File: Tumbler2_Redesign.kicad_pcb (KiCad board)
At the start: 2 copper layers, 77 x 84 mm, 4 parts

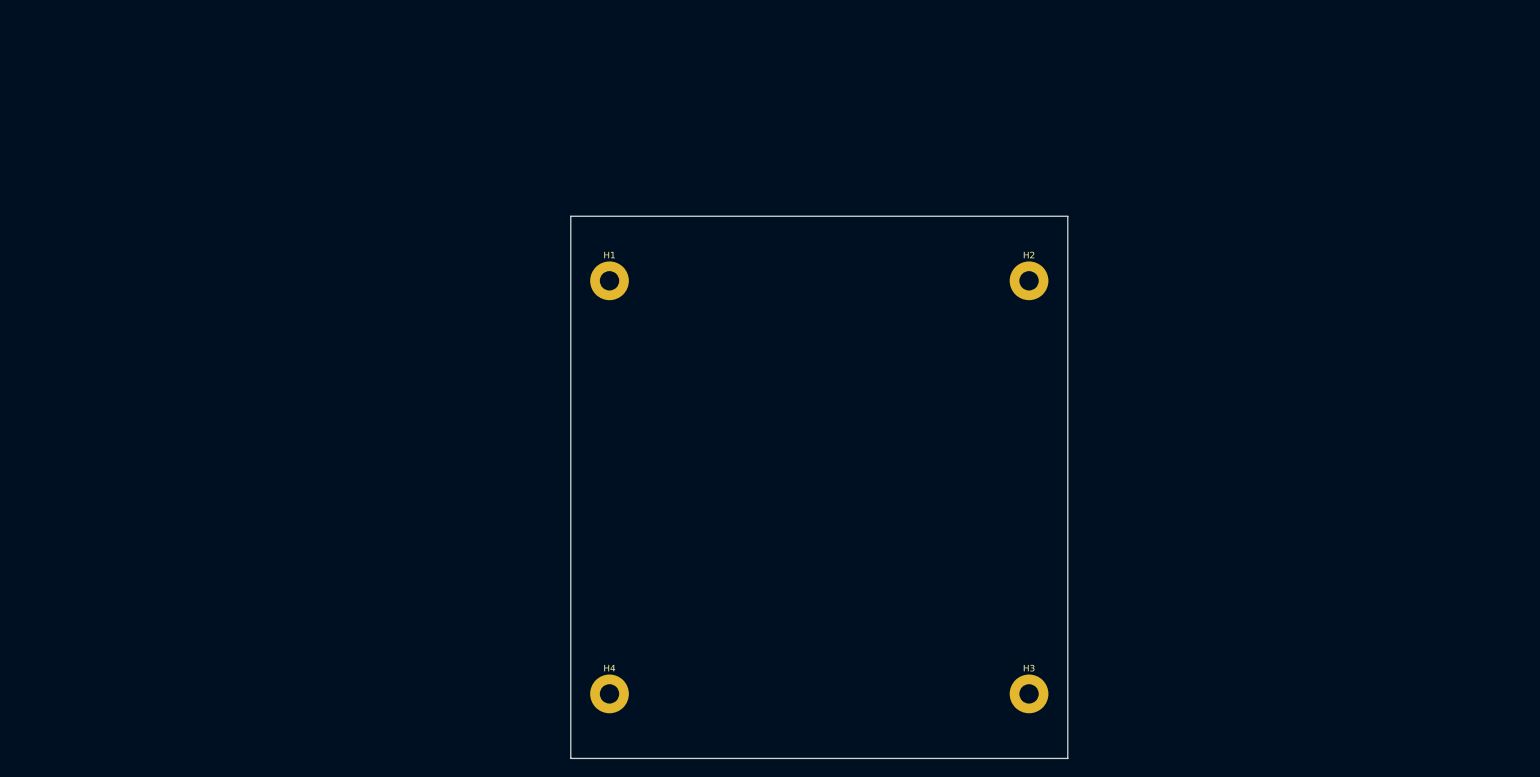
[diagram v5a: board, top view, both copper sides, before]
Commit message: Add components to layout
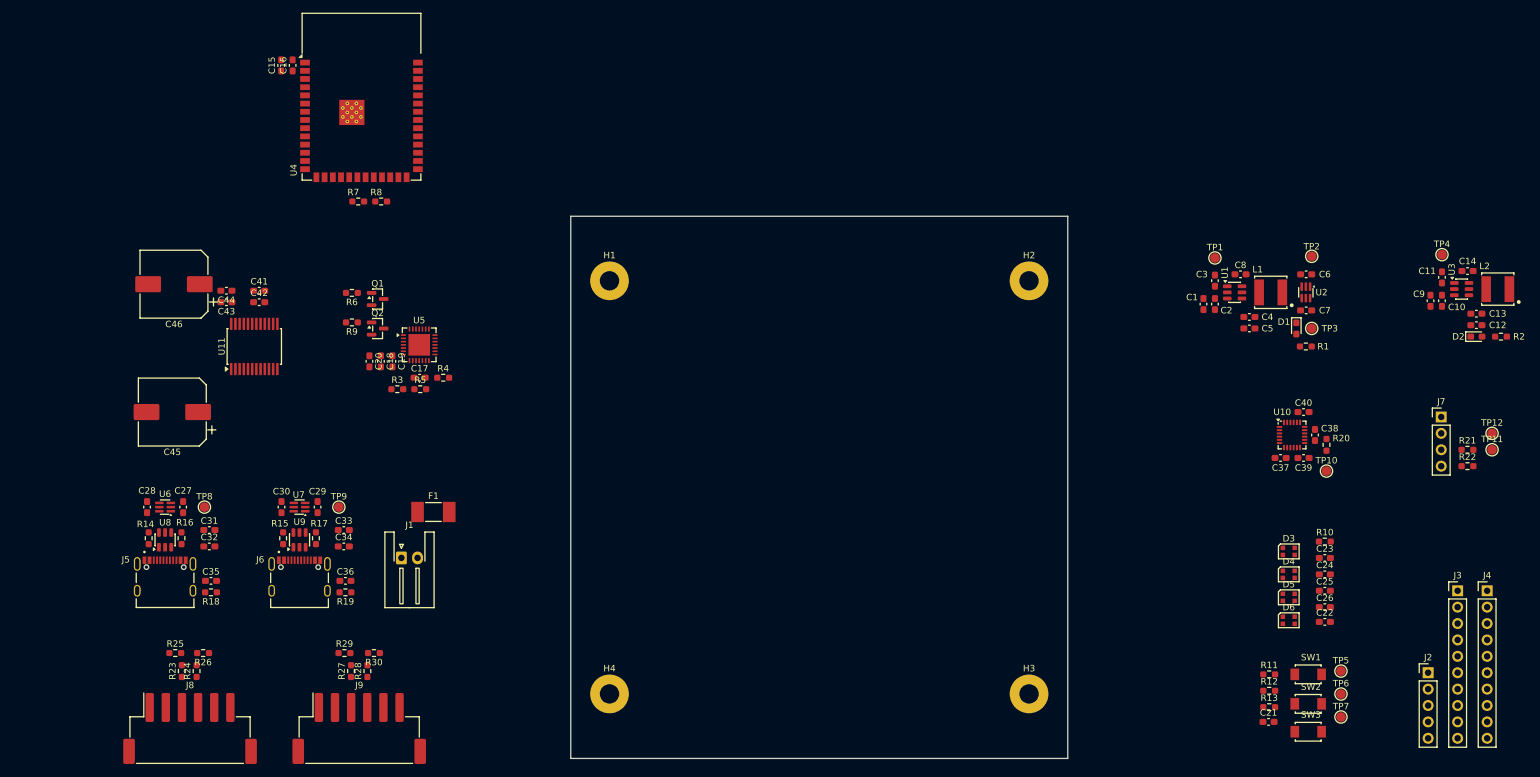
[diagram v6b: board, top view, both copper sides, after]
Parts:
- added C1: 10uF, Capacitor_SMD:C_0603_1608Metric_Pad1.08x0.95mm_HandSolder, F.Cu at (211.8, 75.0)
- added C10: 100nF, Capacitor_SMD:C_0603_1608Metric_Pad1.08x0.95mm_HandSolder, F.Cu at (248.8, 74.5)
- added C11: 100nF, Capacitor_SMD:C_0603_1608Metric_Pad1.08x0.95mm_HandSolder, F.Cu at (248.8, 70.8)
- added C12: 22uF, Capacitor_SMD:C_0603_1608Metric_Pad1.08x0.95mm_HandSolder, F.Cu at (254.1, 78.2)
- added C13: 22uF, Capacitor_SMD:C_0603_1608Metric_Pad1.08x0.95mm_HandSolder, F.Cu at (254.1, 76.5)
- added C14: 100nF, Capacitor_SMD:C_0603_1608Metric_Pad1.08x0.95mm_HandSolder, F.Cu at (252.7, 69.8)
- added C15: 10uF, Capacitor_SMD:C_0603_1608Metric_Pad1.08x0.95mm_HandSolder, F.Cu at (68.9, 38.0)
- added C16: 100nF, Capacitor_SMD:C_0603_1608Metric_Pad1.08x0.95mm_HandSolder, F.Cu at (70.7, 38.0)
- added C17: 1uF, Capacitor_SMD:C_0603_1608Metric_Pad1.08x0.95mm_HandSolder, F.Cu at (90.4, 86.4)
- added C18: 100nF, Capacitor_SMD:C_0603_1608Metric_Pad1.08x0.95mm_HandSolder, F.Cu at (84.4, 83.8)
- added C19: 100nF, Capacitor_SMD:C_0603_1608Metric_Pad1.08x0.95mm_HandSolder, F.Cu at (86.2, 83.8)
- added C2: 100nF, Capacitor_SMD:C_0603_1608Metric_Pad1.08x0.95mm_HandSolder, F.Cu at (213.6, 75.0)
- added C20: 10uF, Capacitor_SMD:C_0603_1608Metric_Pad1.08x0.95mm_HandSolder, F.Cu at (82.6, 83.8)
- added C21: 1uF, Capacitor_SMD:C_0603_1608Metric_Pad1.08x0.95mm_HandSolder, F.Cu at (221.9, 139.7)
- added C22: 100nF, Capacitor_SMD:C_0603_1608Metric_Pad1.08x0.95mm_HandSolder, F.Cu at (230.6, 124.2)
- added C23: 100nF, Capacitor_SMD:C_0603_1608Metric_Pad1.08x0.95mm_HandSolder, F.Cu at (230.6, 114.3)
- added C24: 100nF, Capacitor_SMD:C_0603_1608Metric_Pad1.08x0.95mm_HandSolder, F.Cu at (230.6, 116.8)
- added C25: 100nF, Capacitor_SMD:C_0603_1608Metric_Pad1.08x0.95mm_HandSolder, F.Cu at (230.6, 119.4)
- added C26: 10uF, Capacitor_SMD:C_0603_1608Metric_Pad1.08x0.95mm_HandSolder, F.Cu at (230.6, 121.9)
- added C27: 100nF, Capacitor_SMD:C_0603_1608Metric_Pad1.08x0.95mm_HandSolder, F.Cu at (53.7, 106.4)
- added C28: 100nF, Capacitor_SMD:C_0603_1608Metric_Pad1.08x0.95mm_HandSolder, F.Cu at (48.2, 106.4)
- added C29: 100nF, Capacitor_SMD:C_0603_1608Metric_Pad1.08x0.95mm_HandSolder, F.Cu at (74.6, 106.4)
- added C3: 100nF, Capacitor_SMD:C_0603_1608Metric_Pad1.08x0.95mm_HandSolder, F.Cu at (213.6, 71.3)
- added C30: 100nF, Capacitor_SMD:C_0603_1608Metric_Pad1.08x0.95mm_HandSolder, F.Cu at (69.0, 106.4)
- added C31: 100nF, Capacitor_SMD:C_0603_1608Metric_Pad1.08x0.95mm_HandSolder, F.Cu at (57.8, 110.0)
- added C32: 10uF, Capacitor_SMD:C_0603_1608Metric_Pad1.08x0.95mm_HandSolder, F.Cu at (57.8, 112.5)
- added C33: 100nF, Capacitor_SMD:C_0603_1608Metric_Pad1.08x0.95mm_HandSolder, F.Cu at (78.6, 110.0)
- added C34: 10uF, Capacitor_SMD:C_0603_1608Metric_Pad1.08x0.95mm_HandSolder, F.Cu at (78.6, 112.5)
- added C35: 100nF, Capacitor_SMD:C_0603_1608Metric_Pad1.08x0.95mm_HandSolder, F.Cu at (58.1, 117.8)
- added C36: 100nF, Capacitor_SMD:C_0603_1608Metric_Pad1.08x0.95mm_HandSolder, F.Cu at (78.9, 117.8)
- added C37: 100nF, Capacitor_SMD:C_0603_1608Metric_Pad1.08x0.95mm_HandSolder, F.Cu at (223.8, 98.8)
- added C38: 10nF, Capacitor_SMD:C_0603_1608Metric_Pad1.08x0.95mm_HandSolder, F.Cu at (229.1, 95.2)
- added C39: 100nF, Capacitor_SMD:C_0603_1608Metric_Pad1.08x0.95mm_HandSolder, F.Cu at (227.3, 98.8)
- added C4: 22uF, Capacitor_SMD:C_0603_1608Metric_Pad1.08x0.95mm_HandSolder, F.Cu at (218.9, 77.0)
- added C40: 2.2nF, Capacitor_SMD:C_0603_1608Metric_Pad1.08x0.95mm_HandSolder, F.Cu at (227.3, 91.7)
- added C41: 10uF, Capacitor_SMD:C_0603_1608Metric_Pad1.08x0.95mm_HandSolder, F.Cu at (65.5, 72.9)
- added C42: 100nF, Capacitor_SMD:C_0603_1608Metric_Pad1.08x0.95mm_HandSolder, F.Cu at (65.5, 74.7)
- added C43: 100nF, Capacitor_SMD:C_0603_1608Metric_Pad1.08x0.95mm_HandSolder, F.Cu at (60.5, 74.7)
- added C44: 10uF, Capacitor_SMD:C_0603_1608Metric_Pad1.08x0.95mm_HandSolder, F.Cu at (60.5, 72.9)
- added C45: 220uF, Capacitor_SMD:CP_Elec_10x10, F.Cu at (52.1, 91.7)
- added C46: 220uF, Capacitor_SMD:CP_Elec_10x10, F.Cu at (52.3, 71.9)
- added C5: 22uF, Capacitor_SMD:C_0603_1608Metric_Pad1.08x0.95mm_HandSolder, F.Cu at (218.9, 78.7)
- added C6: 100nF, Capacitor_SMD:C_0603_1608Metric_Pad1.08x0.95mm_HandSolder, F.Cu at (227.7, 70.4)
- added C7: 100nF, Capacitor_SMD:C_0603_1608Metric_Pad1.08x0.95mm_HandSolder, F.Cu at (227.7, 75.9)
- added C8: 100nF, Capacitor_SMD:C_0603_1608Metric_Pad1.08x0.95mm_HandSolder, F.Cu at (217.6, 70.4)
- added C9: 10uF, Capacitor_SMD:C_0603_1608Metric_Pad1.08x0.95mm_HandSolder, F.Cu at (247.0, 74.5)
- added D1: LED, LED_SMD:LED_0603_1608Metric_Pad1.05x0.95mm_HandSolder, F.Cu at (226.2, 78.7)
- added D2: LED, LED_SMD:LED_0603_1608Metric_Pad1.05x0.95mm_HandSolder, F.Cu at (254.1, 80.0)
- added D3: WS2812B, LED_SMD:LED_WS2812B-2020_PLCC4_2.0x2.0mm, F.Cu at (225.0, 113.3)
- added D4: WS2812B, LED_SMD:LED_WS2812B-2020_PLCC4_2.0x2.0mm, F.Cu at (225.0, 116.8)
- added D5: WS2812B, LED_SMD:LED_WS2812B-2020_PLCC4_2.0x2.0mm, F.Cu at (225.0, 120.4)
- added D6: WS2812B, LED_SMD:LED_WS2812B-2020_PLCC4_2.0x2.0mm, F.Cu at (225.0, 124.0)
- added F1: 5A, Fuse:Fuse_Littelfuse-NANO2-451_453, F.Cu at (92.5, 107.2)
- added J1: Conn_01x02, Connector_JST:JST_XH_S2B-XH-A-1_1x02_P2.50mm_Horizontal, F.Cu at (87.6, 114.3)
- added J2: Conn_01x05, Connector_PinHeader_2.54mm:PinHeader_1x05_P2.54mm_Vertical, F.Cu at (246.6, 132.1)
- added J3: Conn_01x10, Connector_PinHeader_2.54mm:PinHeader_1x10_P2.54mm_Vertical, F.Cu at (251.2, 119.4)
- added J4: Conn_01x10, Connector_PinHeader_2.54mm:PinHeader_1x10_P2.54mm_Vertical, F.Cu at (255.8, 119.4)
- added J5: USB_C_Receptacle_USB2.0_16P, Tumbler2:KINGHELM_KH-TYPE-C-16P, F.Cu at (51.0, 119.4)
- added J6: USB_C_Receptacle_USB2.0_16P, Tumbler2:KINGHELM_KH-TYPE-C-16P, F.Cu at (71.8, 119.4)
- added J7: Conn_01x04, Connector_PinHeader_2.54mm:PinHeader_1x04_P2.54mm_Vertical, F.Cu at (248.7, 92.5)
- added J8: Conn_01x06, Connector_JST:JST_XH_S6B-XH-SM4-TB_1x06-1MP_P2.50mm_Horizontal, F.Cu at (54.8, 140.7)
- added J9: Conn_01x06, Connector_JST:JST_XH_S6B-XH-SM4-TB_1x06-1MP_P2.50mm_Horizontal, F.Cu at (81.0, 140.7)
- added L1: 4.7uH, Tumbler2:VLS5045EX-4R7M, F.Cu at (222.2, 73.2)
- added L2: 4.7uH, Tumbler2:VLS5045EX-4R7M, F.Cu at (257.4, 72.6)
- added Q1: BC817, Package_TO_SOT_SMD:SOT-23, F.Cu at (83.9, 74.2)
- added Q2: BC817, Package_TO_SOT_SMD:SOT-23, F.Cu at (83.9, 78.8)
- added R1: 680, Resistor_SMD:R_0603_1608Metric_Pad0.98x0.95mm_HandSolder, F.Cu at (227.7, 81.5)
- added R10: 10k, Resistor_SMD:R_0603_1608Metric_Pad0.98x0.95mm_HandSolder, F.Cu at (230.6, 111.8)
- added R11: 10k, Resistor_SMD:R_0603_1608Metric_Pad0.98x0.95mm_HandSolder, F.Cu at (222.0, 132.3)
- added R12: 10k, Resistor_SMD:R_0603_1608Metric_Pad0.98x0.95mm_HandSolder, F.Cu at (222.0, 134.9)
- added R13: 10k, Resistor_SMD:R_0603_1608Metric_Pad0.98x0.95mm_HandSolder, F.Cu at (222.0, 137.4)
- added R14: 5k1, Resistor_SMD:R_0603_1608Metric_Pad0.98x0.95mm_HandSolder, F.Cu at (48.4, 111.2)
- added R15: 5k1, Resistor_SMD:R_0603_1608Metric_Pad0.98x0.95mm_HandSolder, F.Cu at (69.2, 111.2)
- added R16: 5k1, Resistor_SMD:R_0603_1608Metric_Pad0.98x0.95mm_HandSolder, F.Cu at (53.5, 111.2)
- added R17: 5k1, Resistor_SMD:R_0603_1608Metric_Pad0.98x0.95mm_HandSolder, F.Cu at (74.3, 111.2)
- added R18: 1M, Resistor_SMD:R_0603_1608Metric_Pad0.98x0.95mm_HandSolder, F.Cu at (58.1, 119.6)
- added R19: 1M, Resistor_SMD:R_0603_1608Metric_Pad0.98x0.95mm_HandSolder, F.Cu at (78.9, 119.6)
- added R2: 470, Resistor_SMD:R_0603_1608Metric_Pad0.98x0.95mm_HandSolder, F.Cu at (257.9, 80.0)
- added R20: 10k, Resistor_SMD:R_0603_1608Metric_Pad0.98x0.95mm_HandSolder, F.Cu at (230.9, 96.8)
- added R21: 1k8, Resistor_SMD:R_0603_1608Metric_Pad0.98x0.95mm_HandSolder, F.Cu at (252.7, 97.5)
- added R22: 3k3, Resistor_SMD:R_0603_1608Metric_Pad0.98x0.95mm_HandSolder, F.Cu at (252.7, 100.1)
- added R23: 1k8, Resistor_SMD:R_0603_1608Metric_Pad0.98x0.95mm_HandSolder, F.Cu at (53.5, 131.8)
- added R24: 1k8, Resistor_SMD:R_0603_1608Metric_Pad0.98x0.95mm_HandSolder, F.Cu at (55.8, 131.8)
- added R25: 3k3, Resistor_SMD:R_0603_1608Metric_Pad0.98x0.95mm_HandSolder, F.Cu at (52.5, 129.0)
- added R26: 3k3, Resistor_SMD:R_0603_1608Metric_Pad0.98x0.95mm_HandSolder, F.Cu at (56.8, 129.0)
- added R27: 1k8, Resistor_SMD:R_0603_1608Metric_Pad0.98x0.95mm_HandSolder, F.Cu at (79.8, 131.8)
- added R28: 1k8, Resistor_SMD:R_0603_1608Metric_Pad0.98x0.95mm_HandSolder, F.Cu at (82.3, 131.8)
- added R29: 3k3, Resistor_SMD:R_0603_1608Metric_Pad0.98x0.95mm_HandSolder, F.Cu at (78.7, 129.0)
- added R3: 22k1, Resistor_SMD:R_0603_1608Metric_Pad0.98x0.95mm_HandSolder, F.Cu at (86.9, 88.2)
- added R30: 3k3, Resistor_SMD:R_0603_1608Metric_Pad0.98x0.95mm_HandSolder, F.Cu at (83.3, 129.0)
- added R4: 1k, Resistor_SMD:R_0603_1608Metric_Pad0.98x0.95mm_HandSolder, F.Cu at (94.0, 86.4)
- added R5: 47k5, Resistor_SMD:R_0603_1608Metric_Pad0.98x0.95mm_HandSolder, F.Cu at (90.5, 88.2)
- added R6: 10k, Resistor_SMD:R_0603_1608Metric_Pad0.98x0.95mm_HandSolder, F.Cu at (79.9, 73.2)
- added R7: 4k7, Resistor_SMD:R_0603_1608Metric_Pad0.98x0.95mm_HandSolder, F.Cu at (80.9, 59.1)
- added R8: 4k7, Resistor_SMD:R_0603_1608Metric_Pad0.98x0.95mm_HandSolder, F.Cu at (84.4, 59.1)
- added R9: 10k, Resistor_SMD:R_0603_1608Metric_Pad0.98x0.95mm_HandSolder, F.Cu at (79.9, 77.8)
- added SW1: SW_Push, Tumbler2:SW_TS-1088-AR02016, F.Cu at (228.0, 132.3)
- added SW2: SW_Push, Tumbler2:SW_TS-1088-AR02016, F.Cu at (228.0, 136.9)
- added SW3: SW_Push, Tumbler2:SW_TS-1088-AR02016, F.Cu at (228.0, 141.2)
- added TP1: TestPoint, TestPoint:TestPoint_Pad_D1.5mm, F.Cu at (213.6, 67.8)
- added TP10: TestPoint, TestPoint:TestPoint_Pad_D1.5mm, F.Cu at (230.9, 100.8)
- added TP11: TestPoint, TestPoint:TestPoint_Pad_D1.5mm, F.Cu at (256.5, 97.5)
- added TP12: TestPoint, TestPoint:TestPoint_Pad_D1.5mm, F.Cu at (256.5, 95.0)
- added TP2: TestPoint, TestPoint:TestPoint_Pad_D1.5mm, F.Cu at (228.6, 67.6)
- added TP3: TestPoint, TestPoint:TestPoint_Pad_D1.5mm, F.Cu at (228.6, 78.7)
- added TP4: TestPoint, TestPoint:TestPoint_Pad_D1.5mm, F.Cu at (248.8, 67.3)
- added TP5: TestPoint, TestPoint:TestPoint_Pad_D1.5mm, F.Cu at (233.1, 131.8)
- added TP6: TestPoint, TestPoint:TestPoint_Pad_D1.5mm, F.Cu at (233.1, 135.4)
- added TP7: TestPoint, TestPoint:TestPoint_Pad_D1.5mm, F.Cu at (233.1, 138.9)
- added TP8: TestPoint, TestPoint:TestPoint_Pad_D1.5mm, F.Cu at (57.0, 106.4)
- added TP9: TestPoint, TestPoint:TestPoint_Pad_D1.5mm, F.Cu at (77.9, 106.4)
- added U1: AP63205WU, Package_TO_SOT_SMD:TSOT-23-6, F.Cu at (216.7, 73.2)
- added U10: MPU-6050, Sensor_Motion:InvenSense_QFN-24_4x4mm_P0.5mm, F.Cu at (225.6, 95.2)
- added U11: TB6612FNG, Package_SO:SSOP-24_5.3x8.2mm_P0.65mm, F.Cu at (64.8, 81.5)
- added U2: LM66100DCK, Package_TO_SOT_SMD:SOT-363_SC-70-6, F.Cu at (227.7, 73.2)
- added U3: AP63203WU, Package_TO_SOT_SMD:TSOT-23-6, F.Cu at (251.8, 72.6)
- added U4: ESP32-S3-WROOM-1, RF_Module:ESP32-S3-WROOM-1, F.Cu at (81.4, 42.8)
- added U5: CP2102N-A02-GQFN28R, Package_DFN_QFN:QFN-28-1EP_5x5mm_P0.5mm_EP3.35x3.35mm, F.Cu at (90.3, 81.3)
- added U6: LM66100DCK, Package_TO_SOT_SMD:SOT-363_SC-70-6, F.Cu at (51.0, 106.4)
- added U7: LM66100DCK, Package_TO_SOT_SMD:SOT-363_SC-70-6, F.Cu at (71.8, 106.4)
- added U8: USBLC6-2SC6, Package_TO_SOT_SMD:SOT-23-6, F.Cu at (51.0, 111.5)
- added U9: USBLC6-2SC6, Package_TO_SOT_SMD:SOT-23-6, F.Cu at (71.8, 111.5)

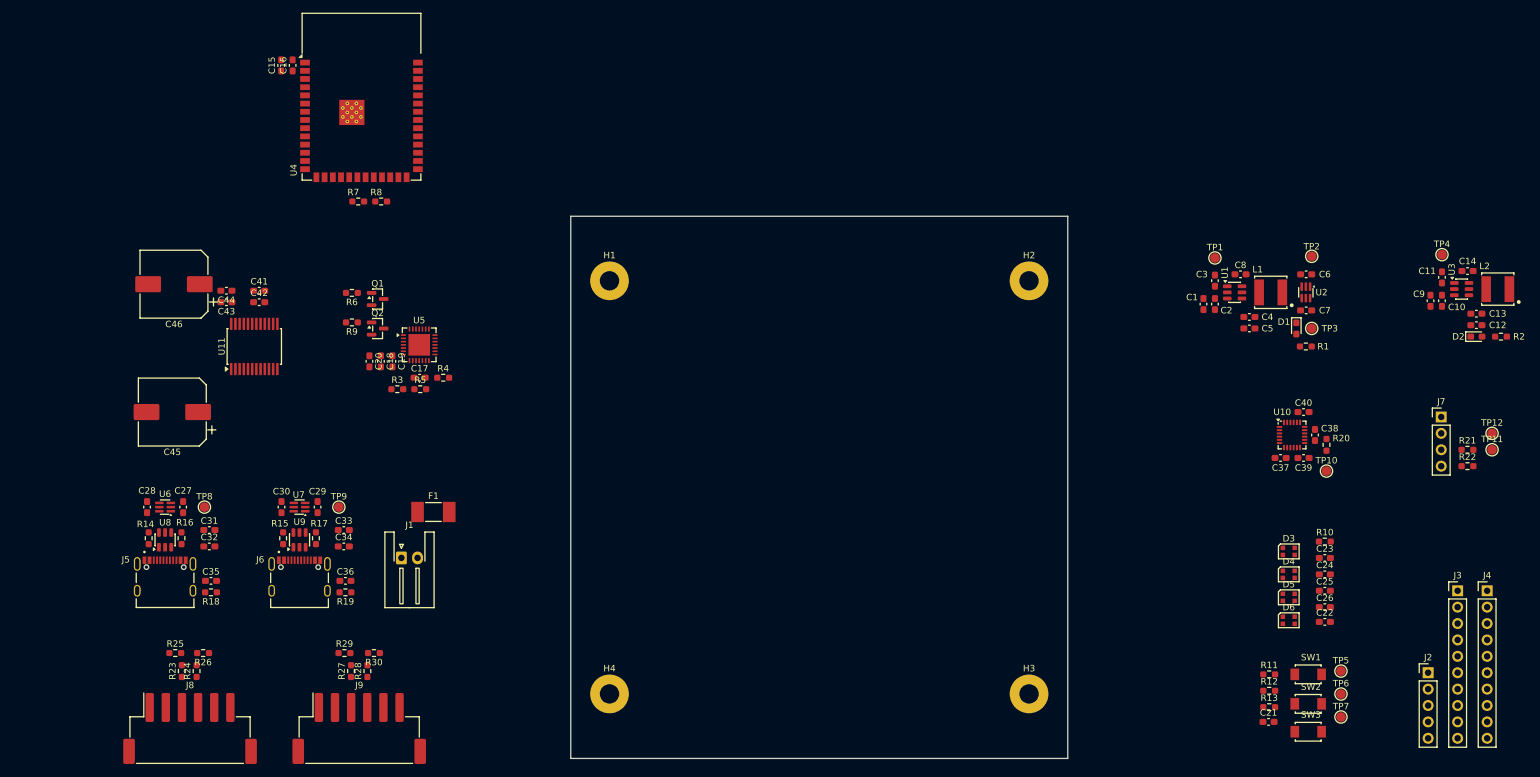
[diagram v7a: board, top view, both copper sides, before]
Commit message: Add missing rgb leds
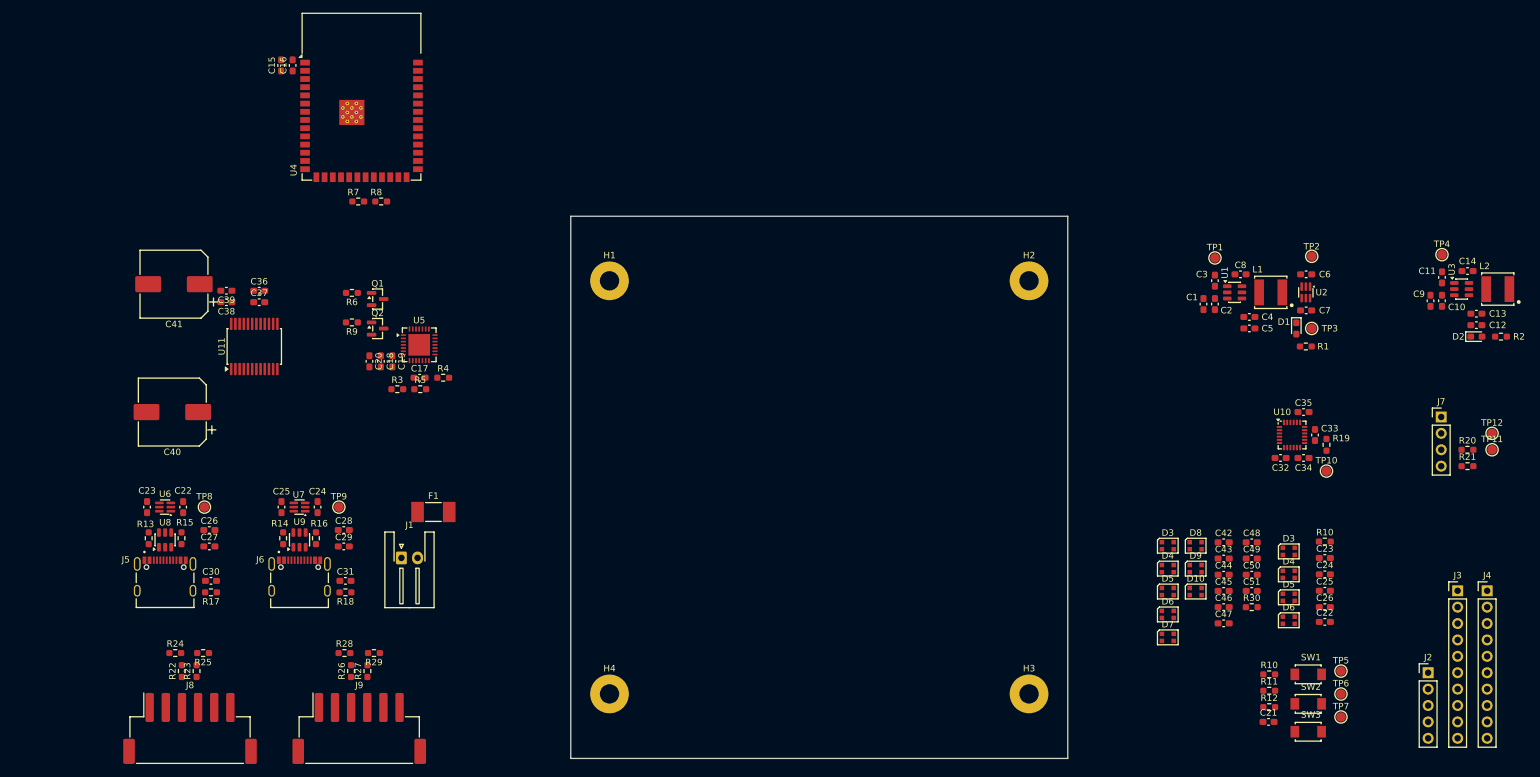
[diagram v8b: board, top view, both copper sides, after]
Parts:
- added C42: 100nF, Capacitor_SMD:C_0603_1608Metric_Pad1.08x0.95mm_HandSolder, F.Cu at (215.0, 111.9)
- added C43: 100nF, Capacitor_SMD:C_0603_1608Metric_Pad1.08x0.95mm_HandSolder, F.Cu at (215.0, 114.4)
- added C44: 100nF, Capacitor_SMD:C_0603_1608Metric_Pad1.08x0.95mm_HandSolder, F.Cu at (215.0, 116.9)
- added C45: 100nF, Capacitor_SMD:C_0603_1608Metric_Pad1.08x0.95mm_HandSolder, F.Cu at (215.0, 119.4)
- added C46: 10uF, Capacitor_SMD:C_0603_1608Metric_Pad1.08x0.95mm_HandSolder, F.Cu at (215.0, 121.9)
- added C47: 100nF, Capacitor_SMD:C_0603_1608Metric_Pad1.08x0.95mm_HandSolder, F.Cu at (215.0, 124.4)
- added C48: 100nF, Capacitor_SMD:C_0603_1608Metric_Pad1.08x0.95mm_HandSolder, F.Cu at (219.3, 111.9)
- added C49: 100nF, Capacitor_SMD:C_0603_1608Metric_Pad1.08x0.95mm_HandSolder, F.Cu at (219.3, 114.4)
- added C50: 100nF, Capacitor_SMD:C_0603_1608Metric_Pad1.08x0.95mm_HandSolder, F.Cu at (219.3, 116.9)
- added C51: 10uF, Capacitor_SMD:C_0603_1608Metric_Pad1.08x0.95mm_HandSolder, F.Cu at (219.3, 119.4)
- added D10: WS2812B, LED_SMD:LED_WS2812B-2020_PLCC4_2.0x2.0mm, F.Cu at (210.6, 119.5)
- added D3: WS2812B, LED_SMD:LED_WS2812B-2020_PLCC4_2.0x2.0mm, F.Cu at (206.3, 112.4)
- added D4: WS2812B, LED_SMD:LED_WS2812B-2020_PLCC4_2.0x2.0mm, F.Cu at (206.3, 116.0)
- added D5: WS2812B, LED_SMD:LED_WS2812B-2020_PLCC4_2.0x2.0mm, F.Cu at (206.3, 119.5)
- added D6: WS2812B, LED_SMD:LED_WS2812B-2020_PLCC4_2.0x2.0mm, F.Cu at (206.3, 123.0)
- added D7: WS2812B, LED_SMD:LED_WS2812B-2020_PLCC4_2.0x2.0mm, F.Cu at (206.3, 126.6)
- added D8: WS2812B, LED_SMD:LED_WS2812B-2020_PLCC4_2.0x2.0mm, F.Cu at (210.6, 112.4)
- added D9: WS2812B, LED_SMD:LED_WS2812B-2020_PLCC4_2.0x2.0mm, F.Cu at (210.6, 116.0)
- added R30: 10k, Resistor_SMD:R_0603_1608Metric_Pad0.98x0.95mm_HandSolder, F.Cu at (219.3, 121.9)
- renumbered C27 to C22, C28 to C23, C29 to C24, C30 to C25, C31 to C26, C32 to C27, C33 to C28, C34 to C29, C35 to C30, C36 to C31, C37 to C32, C38 to C33, C39 to C34, C40 to C35, C41 to C36, C42 to C37, C43 to C38, C44 to C39, C45 to C40, C46 to C41, R11 to R10, R12 to R11, R13 to R12, R14 to R13, R15 to R14, R16 to R15, R17 to R16, R18 to R17, R19 to R18, R20 to R19, R21 to R20, R22 to R21, R23 to R22, R24 to R23, R25 to R24, R26 to R25, R27 to R26, R28 to R27, R29 to R28, R30 to R29
